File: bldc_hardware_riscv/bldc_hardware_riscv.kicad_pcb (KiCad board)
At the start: 4 copper layers, 80 x 60 mm, 126 parts, among them J1 USB_B_Micro, J2 Screw_Terminal_01x06, J3 Screw_Terminal_01x06, J4 Screw_Terminal_01x04, Q1 Q_NMOS_GDS, Q2 Q_NMOS_GDS, Q3 Q_NMOS_GDS, Q4 Q_NMOS_GDS, Q5 Q_NMOS_GDS, Q6 Q_NMOS_GDS, U1 CH32V307VCT6, U101 MAX9919, U102 MAX9919, U103 MAX9919, U2 XL1509-3.3, U3 IC_EG2134, U4 XL7046, U5 MCP1703A-5002_SOT23, U6 MCP1703A-5002_SOT23, U7 SN65HVD230, X1 CON-T, X2 CON-T, X3 CON-T, X4 CON-T, X5 CON-T, Y1 Crystal_GND24

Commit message: First release to PCB manufacture
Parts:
- added AE1: Antenna, BLDC_Library:ANT-F-1-2.4G-0.6MM-FR4, F.Cu at (83.0, 103.2)
- added C39: 0.1uF, Capacitor_SMD:C_0603_1608Metric, F.Cu at (95.7, 103.0)
- added C40: 0.1uF, Capacitor_SMD:C_0603_1608Metric, F.Cu at (85.8, 101.0)
- added U8: CH9141K, BLDC_Library:HSOP-10-1EP_3.9x4.9mm_P1.27mm_EP2.3x2.3mm, F.Cu at (90.5, 101.5)
- added Y2: Crystal_GND24, BLDC_Library:Oscillator_SMD_Abracon_ASE-4Pin_3.2x2.5mm, F.Cu at (96.0, 100.0)
- moved X1 3.00 mm to (87.0, 111.5)
- moved C103 0.63 mm to (144.4, 111.0)
- moved X2 0.50 mm to (87.0, 134.0)
- moved R20 0.30 mm to (118.0, 125.3)
- moved C36 0.10 mm to (132.2, 83.9)
- moved C3 0.10 mm to (113.8, 86.9)
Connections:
- U1 pad 38: unconnected-(U1-Pad38) -> /BLE_MODE
- U1 pad 45: unconnected-(U1-Pad45) -> /BLE_TX
- U1 pad 46: unconnected-(U1-Pad46) -> /BLE_RX
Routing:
- net /BLE_MODE: track 0.00 -> 73.6 mm, vias 0 -> 3
- net /BLE_RX: track 0.00 -> 69.3 mm, vias 0 -> 3
- net /BLE_TX: track 0.00 -> 67.3 mm, vias 0 -> 3
- net GND: track 56.6 -> 76.7 mm, vias 67 -> 87
- net /3.3V: track 106.7 -> 116.1 mm, vias 11 -> 13
- net Net-(U8-Pad4): track 0.00 -> 4.53 mm
- net Net-(C40-Pad1): track 0.00 -> 2.25 mm
- net Net-(U8-Pad5): track 0.00 -> 2.22 mm
- net /CAN-R: track 45.9 -> 43.8 mm
- net /AIN_VIN: track 54.6 -> 55.5 mm
- net /Driver/5V: track 71.3 -> 70.5 mm
- net /Driver/12V: track 142.5 -> 142.8 mm, vias 4 -> 5
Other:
- outline, holes or cut-outs redrawn
- board text added: "3.3V"
- board text added: "5V"
- board text added: "75V MAX"
- board text added: "ADC"
- board text added: "CANH"
- board text added: "CANL"
- board text added: "GND"
- board text added: "Ground"
- board text added: "HALL1"
- board text added: "HALL2"
- board text added: "HALL3"
- board text added: "New Zealand Design"
- board text added: "Phase A"
- board text added: "Phase B"
- board text added: "Phase C"
- board text added: "RISC-V VESC Controller V1.0"
- board text added: "RX"
- board text added: "SWCK"
- board text added: "SWIO"
- board text added: "Supported by"
- board text added: "TX"
- board text added: "Temp"
- board text added: "UBCO"
- board text added: "bikes"
- board text added: "github.com/xu7wong/bldc_hardware_riscv"

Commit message: fix resistor/inductor/capacitor parameters, add boot button, add 120Ohm CAN bus load resistor.
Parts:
- added R40: 2K2, Resistor_SMD:R_0603_1608Metric, F.Cu at (132.4, 98.7)
- added R41: 2K2, Resistor_SMD:R_0603_1608Metric, F.Cu at (144.8, 82.1)
- added R42: 120, Resistor_SMD:R_0805_2012Metric, F.Cu at (103.5, 95.5)
- added SW1: B3U-1000P, Button_Switch_SMD:SW_SPST_B3U-1000P, B.Cu at (130.2, 96.3)
- C17: value 220uF/25V -> 330uF/16V
- C39: value 0.1uF -> 2.2uF
- C5: value 47uF/80V -> 22uF/80V
- C9: value 47uF/6.3V -> 100uF/6.3V
- D3: value PMEG6020AELR -> DSS34
- D6, D8, D9: value 1N4448W -> ES1002FL Panjit; footprint Diode_SMD:D_SOD-123 -> Diode_SMD:D_SOD-123F
- D7: value US1B -> ES1B
- J1: value USB_B_Micro -> USB_B_Micro Vertical
- J2, J3: value Screw_Terminal_01x06 -> 2.00mm JST 6Pin
- J4: value Screw_Terminal_01x04 -> 2.54mm 4Pin
- L1: value 47uH -> 100uH/1.5A
- L2: value 47uH -> 33uH/1A
- Q1, Q2, Q3, Q4, Q5, Q6: value Q_NMOS_GDS -> 80V/200A
- R10: value 0.05 -> 0.082
- R38, R39: value 1K -> 2K2
- U2: value XL1509-3.3 -> XL1509-3.3 XLSEMI
- U3: value IC_EG2134 -> EG2134 EG Micro
- U4: value XL7046 -> XL7046 XLSEMI
- U5, U6: value MCP1703A-5002_SOT23 -> RT9058-50GVL Richtek
- Y1: value Crystal_GND24 -> 8MHz 3225
- Y2: value Crystal_GND24 -> 32MHz 3225
- moved R36 1.10 mm to (106.0, 105.6)
- moved R34 0.80 mm to (103.0, 105.3)
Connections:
- U1 pad 37: unconnected-(U1-Pad37) -> Net-(R41-Pad1)
- U1 pad 94: unconnected-(U1-Pad94) -> /BOOT0
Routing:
- net /BOOT0: track 0.00 -> 24.5 mm, vias 0 -> 2
- net /CANH: track 7.52 -> 15.0 mm
- net /3.3V: track 116.1 -> 121.2 mm
- net /CANL: track 7.54 -> 11.3 mm
- net Net-(R41-Pad1): track 0.00 -> 2.42 mm
- net /AIN_VIN: track 55.5 -> 57.6 mm
- net /AIN_VS3: track 45.9 -> 47.7 mm
- net /Driver/72V: track 6.48 -> 5.68 mm
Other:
- board text added: "- TIM1 3-CH SVPWM Output - ADC1, ADC2 Paralell Mode Sampling for V&I - TIM1 Master, TIM2 Slave - TIM2 CC2 triggers ADC1 DMA - TIM2 interrupt synchronizes SVPWM phase"
- board text added: "2022 Jul"
- board text added: "Migrated from VESC"
- board text added: "RISC-V VESC Controller V1.0.1"
- board text added: "Say hello to"
- board text removed: "RISC-V VESC Controller V1.0"
- board text removed: "UBCO"
- board text removed: "bikes"

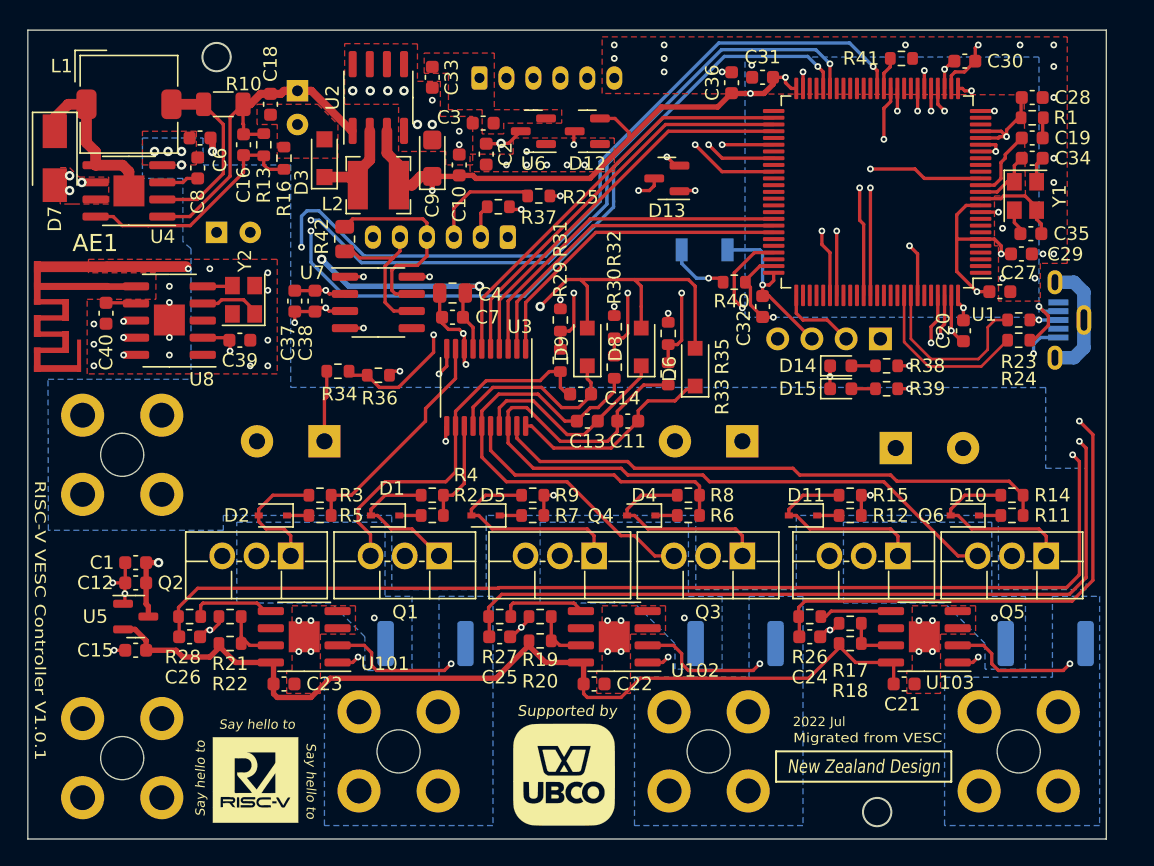
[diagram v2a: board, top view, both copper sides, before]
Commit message: add teardrop by Kicad V6.99
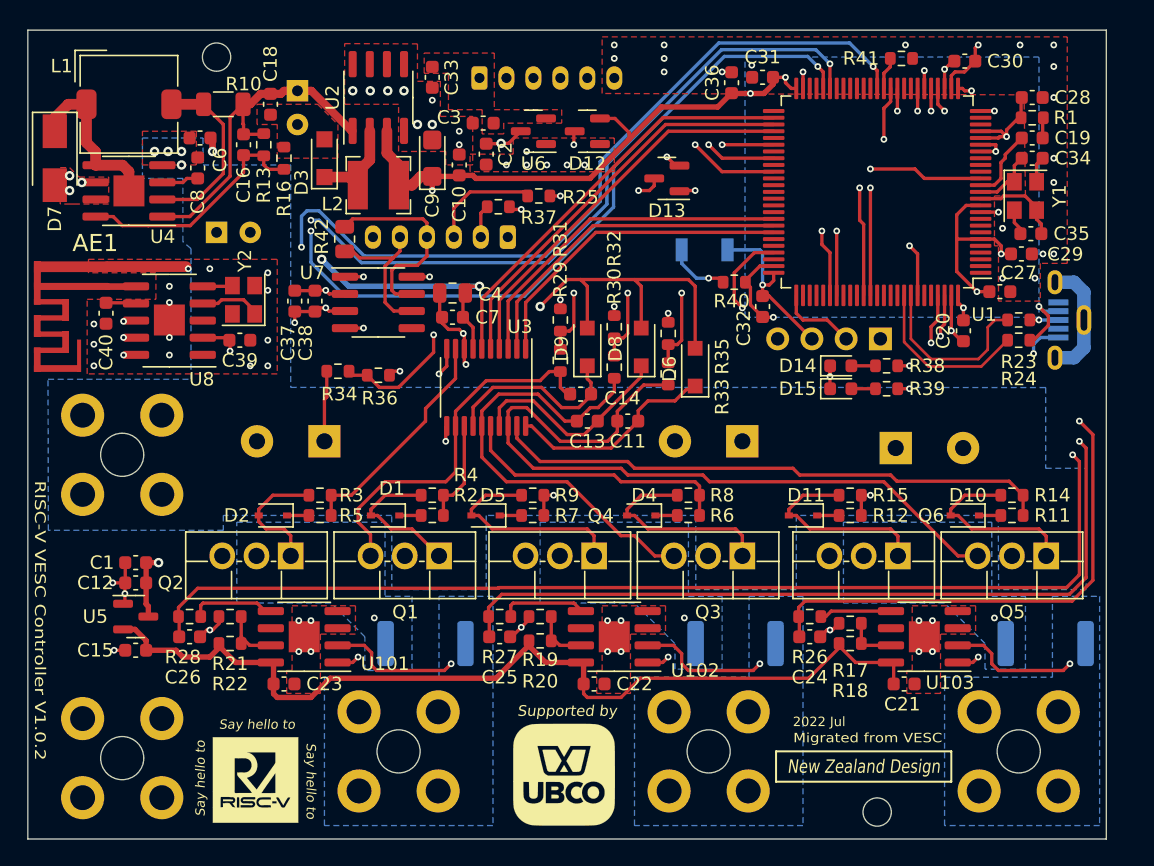
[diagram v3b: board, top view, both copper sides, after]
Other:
- board text added: "RISC-V VESC Controller V1.0.2"
- board text removed: "RISC-V VESC Controller V1.0.1"

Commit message: add debug RX/TX, fix CH9141K footprint error, add 12V detection
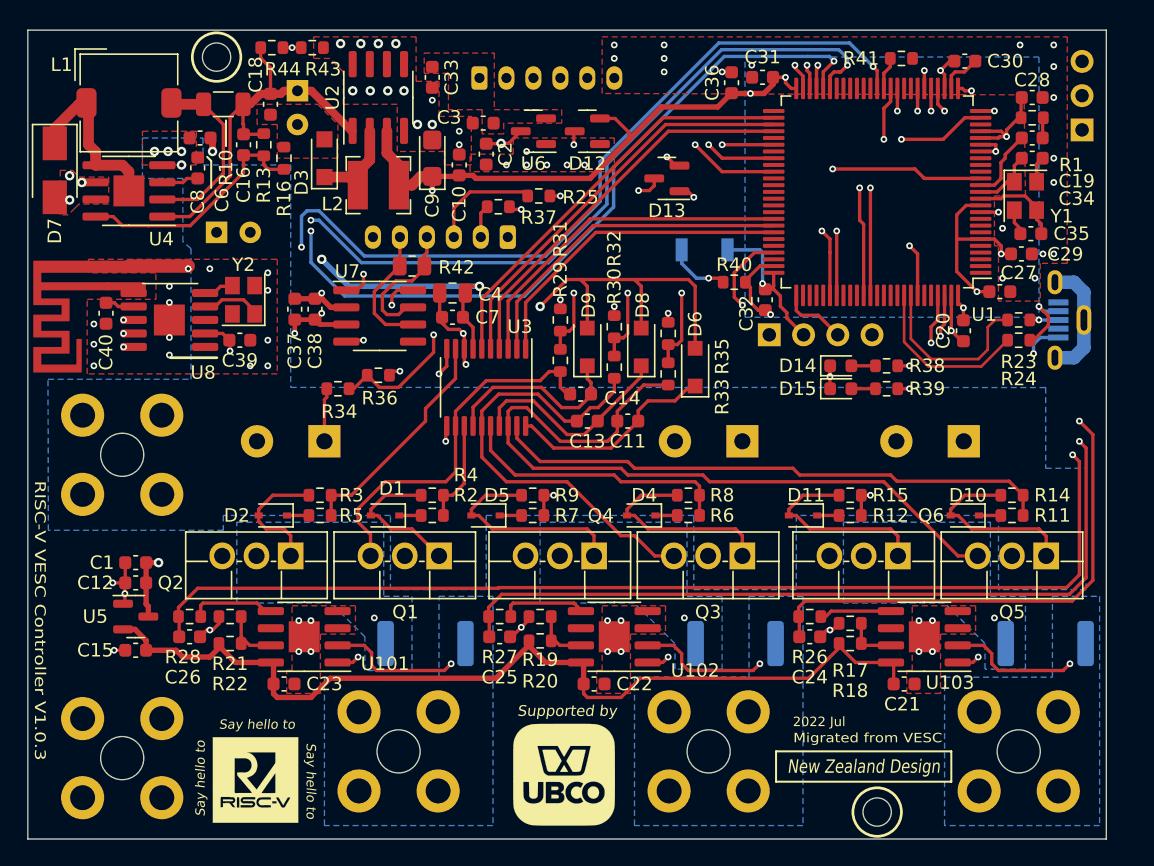
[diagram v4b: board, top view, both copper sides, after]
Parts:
- added J5: Screw_Terminal_01x03, Connector_PinHeader_2.54mm:PinHeader_1x03_P2.54mm_Vertical, B.Cu at (158.2, 87.4)
- added R43: 2K2, Resistor_SMD:R_0603_1608Metric, F.Cu at (101.1, 81.3)
- added R44: 27K, Resistor_SMD:R_0603_1608Metric, F.Cu at (98.1, 81.3)
- J4: value 2.54mm 4Pin -> Screw_Terminal_01x04
- R101, R102, R103: value 0.0005 -> 0.0003
- R13: value 22K -> 19.1K
- U8: footprint BLDC_Library:HSOP-10-1EP_3.9x4.9mm_P1.27mm_EP2.3x2.3mm -> BLDC_Library:HSOP-10-1EP_3.9x4.9mm_P1.00mm_EP2.3x2.3mm
- moved J4 8.25 mm to (135.0, 102.6), turned to -90 degrees
- moved R42 5.39 mm to (108.5, 97.5), turned to 0 degrees
- moved C103 5.07 mm to (149.4, 110.5), turned to 180 degrees
- moved R34 1.30 mm to (103.0, 106.6)
- moved U7 1.00 mm to (106.1, 101.2)
- moved D7 0.90 mm to (82.0, 90.4)
- moved C37 0.60 mm to (99.8, 100.7)
- moved C38 0.60 mm to (101.3, 100.7)
- moved C32 0.54 mm to (134.7, 100.0)
- moved L1 0.10 mm to (87.5, 85.4)
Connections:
- net Net-(R41-Pad1) renamed /BOOT1
- J4 pad 1: /SWIO -> GND
- J4 pad 2: /SWCK -> /3.3V
- J4 pad 3: /3.3V -> /SWCK
- J4 pad 4: GND -> /SWIO
- U1 pad 24: unconnected-(U1-Pad24) -> /AIN_V12V
- U1 pad 47: unconnected-(U1-Pad47) -> /DEBUG_TX
- U1 pad 48: unconnected-(U1-Pad48) -> /DEBUG_RX
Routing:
- net /AIN_V12V: track 0.00 -> 59.6 mm, vias 0 -> 2
- net /DEBUG_RX: track 0.00 -> 24.0 mm, vias 0 -> 1
- net /DEBUG_TX: track 0.00 -> 23.8 mm, vias 0 -> 1
- net GND: track 77.0 -> 61.3 mm, vias 87 -> 89
- net /CANH: track 15.0 -> 10.1 mm
- net /BLE_TX: track 67.3 -> 69.8 mm
- net /CAN-R: track 43.8 -> 45.8 mm
- net /Driver/12V: track 142.8 -> 144.7 mm
- net /CANL: track 11.3 -> 9.66 mm
- net /BLE_RX: track 69.3 -> 70.8 mm
- net /Driver/72V: track 5.68 -> 4.38 mm
- net /AIN_VIN: track 57.6 -> 58.7 mm
- net /ADC_EXT: track 39.8 -> 38.8 mm
- net /SWIO: track 17.6 -> 16.7 mm
- net /SWCK: track 5.81 -> 4.95 mm
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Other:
- board text added: "Debug RX"
- board text added: "Debug TX"
- board text added: "RISC-V VESC Controller V1.0.3"
- board text removed: "RISC-V VESC Controller V1.0.2"

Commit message: fix PCB DRC error, fix CH9141K 3D preview
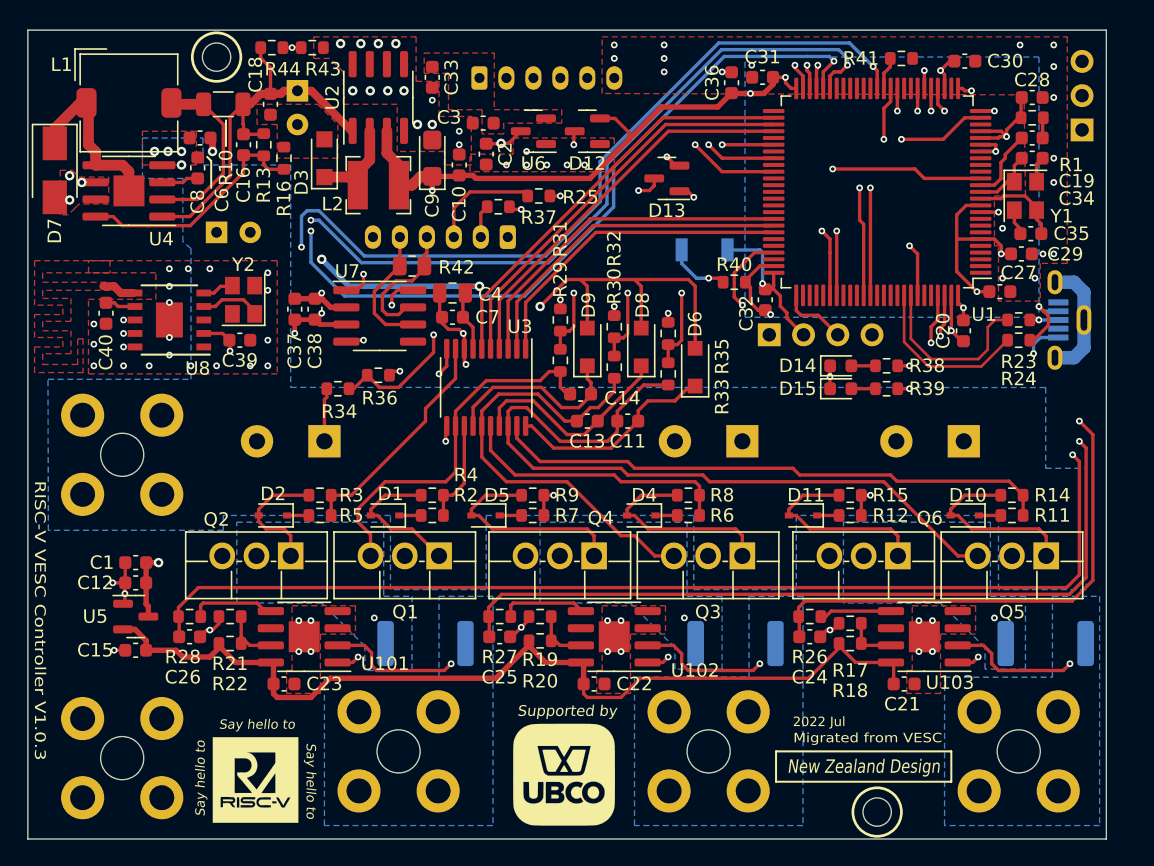
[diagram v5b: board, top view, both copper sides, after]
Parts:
- removed AE1: Antenna, BLDC_Library:ANT-F-1-2.4G-0.6MM-FR4
- U8: footprint BLDC_Library:HSOP-10-1EP_3.9x4.9mm_P1.00mm_EP2.3x2.3mm -> BLDC_Library:SSOP-10_3.9x4.9mm_P1.00mm
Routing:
- net GND: track 61.3 -> 56.2 mm, vias 89 -> 94
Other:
- board text added: "BOOT0"
